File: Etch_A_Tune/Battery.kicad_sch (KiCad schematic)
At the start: 26 parts, among them U1 BQ297xy, U2 CSD16406Q3, U3 CSD16406Q3, U6 BQ25170DSGR

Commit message: Another Update! :D
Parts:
- renumbered C1 to C2, C2 to C3, C3 to C4, R36 to R10, R38 to R11, R35 to R12, R26 to R13, R3 to R14, R4 to R15, R32 to R16, R33 to R17, R34 to R18, R28 to R5, R1 to R6, R2 to R7, R31 to R8, R37 to R9, TP3 to TP23, TP4 to TP24, TP5 to TP25, TP6 to TP26, U6 to U1, U1 to U2, U2 to U4

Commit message: pdf docs
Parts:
- renumbered C2 to C1, C3 to C2, C4 to C3, R6 to R1, R7 to R2, R13 to R26, R5 to R28, R14 to R3, R8 to R31, R16 to R32, R17 to R33, R18 to R34, R12 to R35, R10 to R36, R9 to R37, R11 to R38, R15 to R4, TP23 to TP3, TP24 to TP4, TP25 to TP5, TP26 to TP6, U2 to U1, U4 to U2, U1 to U6

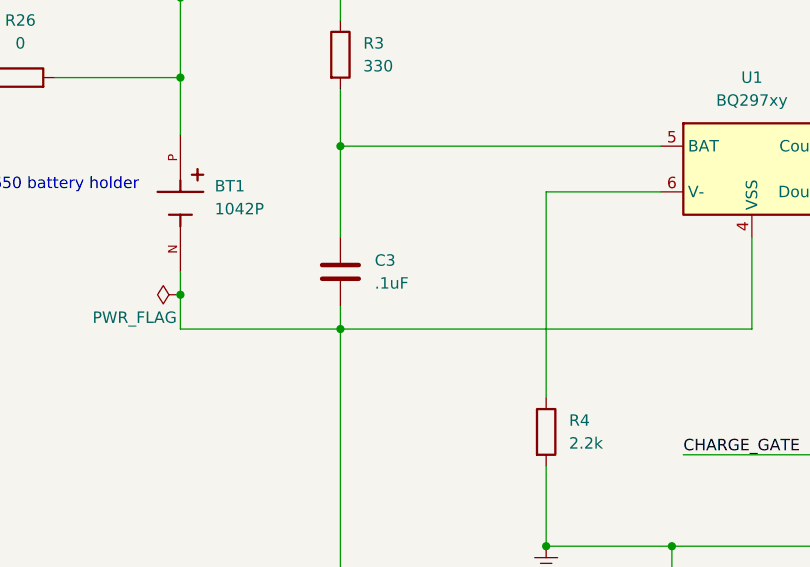
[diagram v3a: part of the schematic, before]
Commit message: Updated BOM
Changed Values for an accurate BOM, and exported results
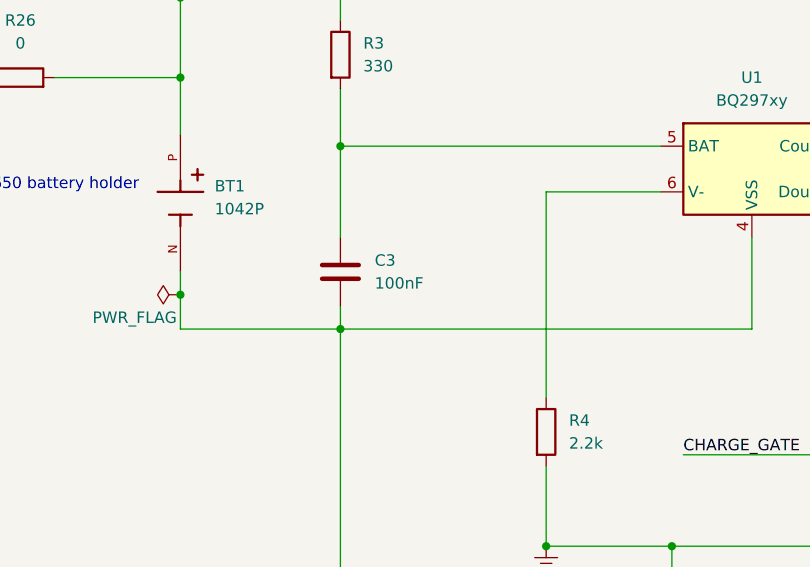
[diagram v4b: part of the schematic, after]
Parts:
- BT1: Arrow Part Number (none) -> BATTERY HOLDER 18650 SMD; DIGIKEY-PURCHASE-URL (none) -> https://www.digikey.com/en/products/detail/keystone-electro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; Dist (none) -> Digikey; Dist Part Number (none) -> 36-1042P-ND; Manufacturer_Name (none) -> Keystone Electronics; Manufacturer_Part_Number (none) -> 1042P; Price (none) -> $5.54
- C1, C2: DIGIKEY-PURCHASE-URL (none) -> https://www.digikey.com/en/products/detail/samsung-electro-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; Dist (none) -> Digikey; Dist Part Number (none) -> 1276-1184-1-ND; Manufacturer_Name (none) -> Samsung Electro-Mechanics; Manufacturer_Part_Number (none) -> CL10B105KA8NNNC; Price (none) -> $0.08
- C3: value .1uF -> 100nF; DIGIKEY-PURCHASE-URL (none) -> https://www.digikey.com/en/products/detail/samsung-electro-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; Dist (none) -> Digikey; Dist Part Number (none) -> 1276-CL10E104KC8VPNCCT-ND; Manufacturer_Name (none) -> Samsung Electro-Mechanics; Manufacturer_Part_Number (none) -> CL10E104KC8VPNC; Price (none) -> $0.25
- R1: DIGIKEY-PURCHASE-URL (none) -> https://www.digikey.com/short/hvhr4nrr; Dist (none) -> Digikey; Dist Part Number (none) -> A129705CT-ND; Manufacturer_Name (none) -> TE Connectivity Passive Product; Manufacturer_Part_Number (none) -> CRGCQ0603F27K; Price (none) -> $0.10
- R2: DIGIKEY-PURCHASE-URL (none) -> https://www.digikey.com/short/8db858df; Dist (none) -> Digikey; Dist Part Number (none) -> P604DBCT-ND; Manufacturer_Name (none) -> Panasonic Electronic Components; Manufacturer_Part_Number (none) -> ERA-3AEB6040V; Price (none) -> $0.10
- R26, R28, R32, R33, R34, R35, R36, R37, R38: DIGIKEY-PURCHASE-URL (none) -> https://www.digikey.com/short/7nbcpfpb; Dist (none) -> Digikey; Dist Part Number (none) -> 311-0.0GRCT-ND; Manufacturer_Name (none) -> YAGEO; Manufacturer_Part_Number (none) -> RC0603JR-070RL; Price (none) -> $0.10
- R3: DIGIKEY-PURCHASE-URL (none) -> https://www.digikey.com/short/brtmprqw; Dist (none) -> Digikey; Dist Part Number (none) -> 311-330GRCT-ND; Manufacturer_Name (none) -> YAGEO; Manufacturer_Part_Number (none) -> RC0603JR-07330RL; Price (none) -> $0.10
- R31: DIGIKEY-PURCHASE-URL (none) -> https://www.digikey.com/short/m3dw570p; Dist (none) -> Digikey; Dist Part Number (none) -> 311-10.0KHRCT-ND; Manufacturer_Name (none) -> YAGEO; Manufacturer_Part_Number (none) -> RC0603FR-0710KL; Price (none) -> $0.10
- R4: DIGIKEY-PURCHASE-URL (none) -> https://www.digikey.com/short/dd50bd49; Dist (none) -> Digikey; Dist Part Number (none) -> 311-2.2KGRCT-ND; Manufacturer_Name (none) -> YAGEO; Manufacturer_Part_Number (none) -> RC0603JR-072K2L; Price (none) -> $0.11
- TP3, TP4, TP5, TP6: Dist (none) -> Digikey; now left out of the parts list
- U1: DIGIKEY-PURCHASE-URL (none) -> https://www.digikey.com/short/0pdtmq92; Dist (none) -> Digikey; Dist Part Number (none) -> 296-43985-1-ND; Manufacturer_Name (none) -> Texas Instruments; Manufacturer_Part_Number (none) -> BQ29700DSER; Price (none) -> $0.51
- U2, U3: DIGIKEY-PURCHASE-URL https://snapeda.com/shop?store=DigiKey&id=288071 -> https://www.digikey.com/short/1w7db9w0; Dist (none) -> Digikey; Dist Part Number (none) -> 296-24251-1-ND; Manufacturer_Name (none) -> Texas Instruments; Manufacturer_Part_Number (none) -> CSD16406Q3; Price (none) -> $1.65
- U6: DIGIKEY-PURCHASE-URL (none) -> https://www.digikey.com/short/rmtzphqd; Dist (none) -> Digikey; Dist Part Number (none) -> 296-BQ25170DSGRCT-ND; Manufacturer_Name (none) -> Texas Instruments; Manufacturer_Part_Number (none) -> BQ25170DSGR; Price (none) -> $0.96
